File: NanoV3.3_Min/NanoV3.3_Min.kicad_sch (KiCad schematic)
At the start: 27 parts, among them IC1 FT232RL, IC3 328P-MUR, J1 Conn_1x15, J2 Conn_1x15, J3 Conn_Mini_USB, Y1 16MHz

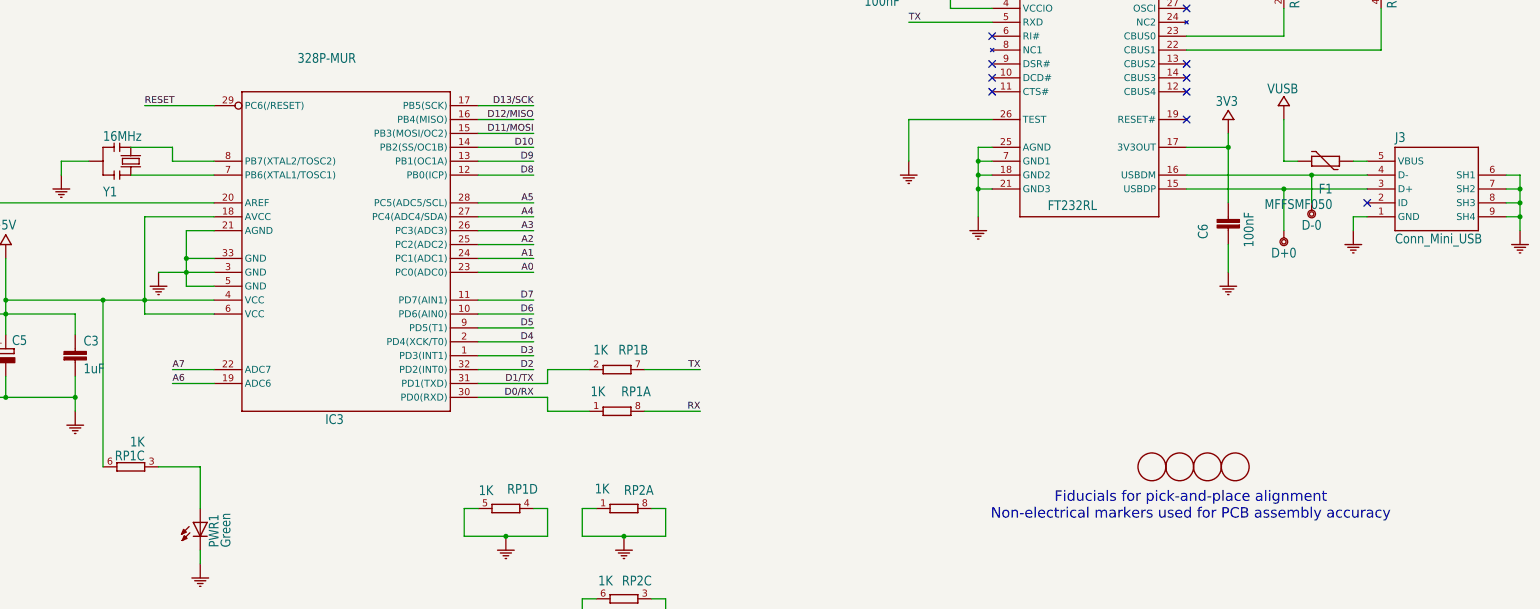
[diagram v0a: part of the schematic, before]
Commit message: finalized first iteration of nano minima
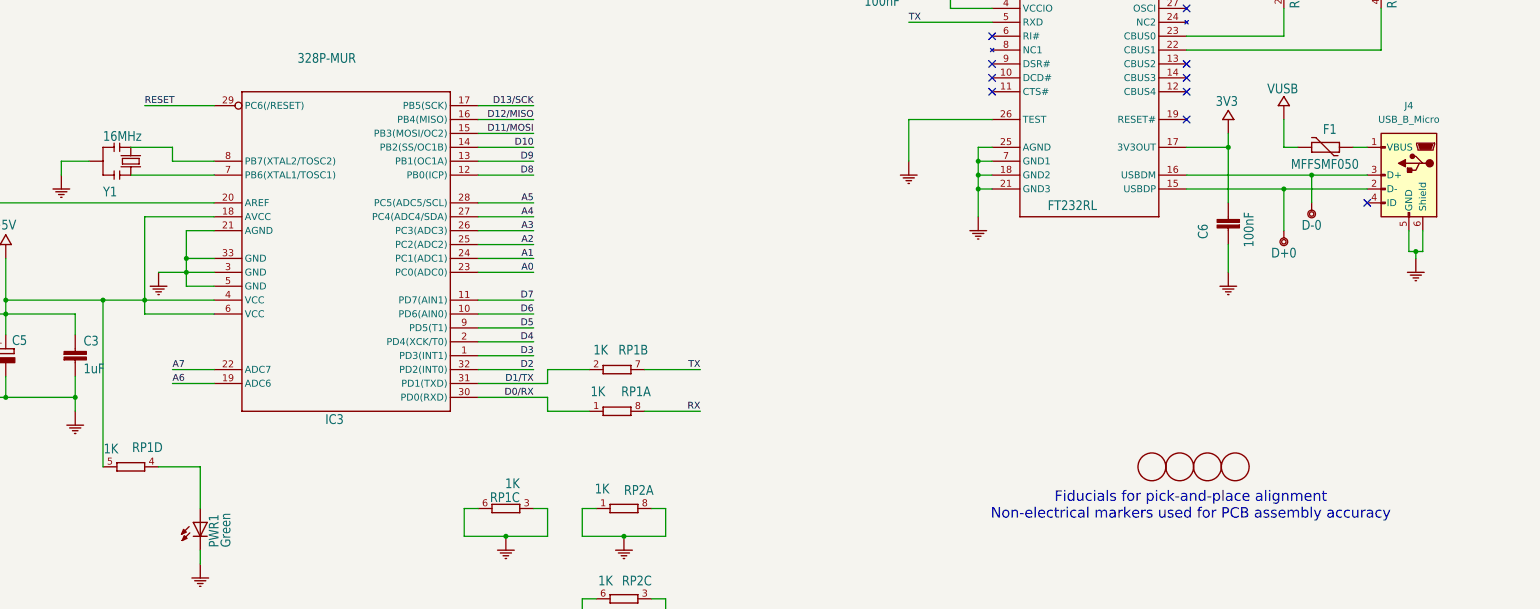
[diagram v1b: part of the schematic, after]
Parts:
- removed J3: Conn_Mini_USB, NanoV3.3:USB_Mini-B_Lumberg_2486_01_Horizontal, symbol NanoV3.3:Conn_Mini_USB
- added J4: USB_B_Micro, Connector_USB:USB_Micro-B_Amphenol_10118193-0001LF_Horizontal, symbol Connector:USB_B_Micro
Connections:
- net +5V: now also RP1.5 (2); no longer RP1.6 (2)
- net COM: now also RP1.3 (1), RP1.6 (2), J4.5 (GND), J4.6 (Shield); no longer RP1.4 (1), RP1.5 (2)
- net at D+0.X (P$1), IC1.15 (USBDP): now also J4.2 (D-)
- net at D-0.X (P$1), IC1.16 (USBDM): now also J4.3 (D+)
- net at F1.2: now also J4.1 (VBUS)
- net at PWR1.1: now also RP1.4 (1); no longer RP1.3 (1)
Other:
- moved on the sheet: F1

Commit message: added bom start
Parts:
- removed FD1, FD2, FD3, FD4: DNP, NanoV3.3:Fiducial_1mm_Mask1.5mm, symbol NanoV3.3:Fiducial
- added D6: LED, symbol Device:LED
- LEDG1: renamed from PWR1; value Green -> LTST-C171GKT
- LEDO1: renamed from TX0; value Green -> LTST-C170KFKT
- LEDR1: renamed from RX0; value Red -> LTST-C171KRKT
- renumbered C7 to C2, C5 to C3, C3 to C4, C4 to C5, C2 to C6, C9 to C7, C6 to C8, D+0 to D+1, D-0 to D-1, IC3 to IC1, IC1 to IC2, J4 to J3
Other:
- note removed: "Fiducials for pick-and-place alignment Non-electrical markers used for PCB assembly accuracy"
- moved on the sheet: C6, C7, RP2B
